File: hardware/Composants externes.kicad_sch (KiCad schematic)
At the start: 0 parts

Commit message: Erreur de manipulation, version 2.3 ok
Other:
- note added: "Nappe communication I2C avec FRDM-IMX8MP ------------------------------------------------------------ Reference Fabriquant qté Remarque IDSD-05-D-03.00-T-G Samtec 1 Nappe IDC 5*2 pins, 3 pouces de long IDSD-05-D-04.00-T-G Samtec 1 Nappe IDC 5*2 pins, 4 pouces de long"
- note removed: "Nappe communication I2C avec FRDM-IMX8MP ------------------------------------------------------------ Reference Fabriquant qté Remarque IDSD-05-D-02.00-T-G Samtec 1 Nappe IDC 5*2 pins, 5cm de long"
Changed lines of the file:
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@@
 		)
 	)
-	(text "Nappe communication I2C avec FRDM-IMX8MP\n------------------------------------------------------------\nReference              Fabriquant       qté          Remarque\nIDSD-05-D-02.00-T-G    Samtec           1            Nappe IDC 5*2 pins, 5cm de long"
+	(text "Nappe communication I2C avec FRDM-IMX8MP\n------------------------------------------------------------\nReference              Fabriquant       qté          Remarque\nIDSD-05-D-03.00-T-G    Samtec           1            Nappe IDC 5*2 pins, 3 pouces de long\nIDSD-05-D-04.00-T-G    Samtec           1            Nappe IDC 5*2 pins, 4 pouces de long"
 		(exclude_from_sim no)
 		(at 19.304 99.568 0)

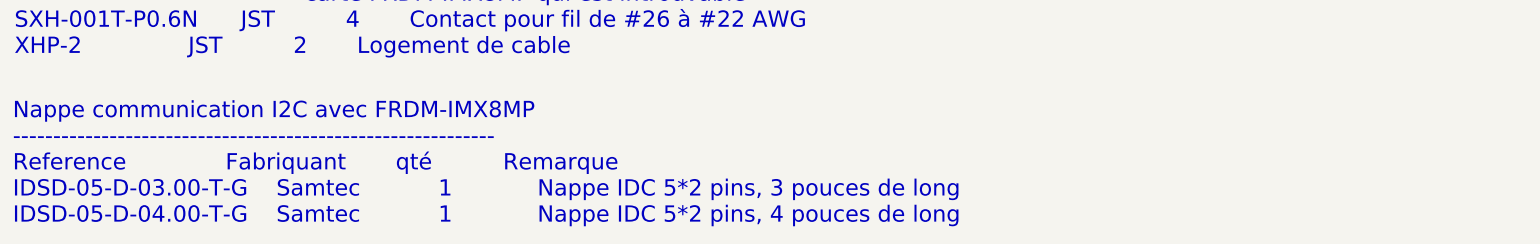
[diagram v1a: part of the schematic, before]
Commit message: V2.3b: correction sur la nomenclature (bom) de plusieurs composants, suppression d'une mauvaise manipulation precedente
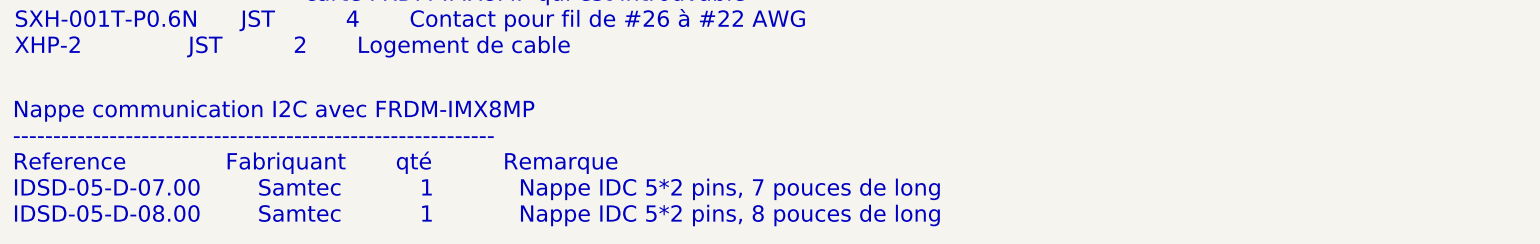
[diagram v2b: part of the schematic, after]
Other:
- note added: "Nappe communication I2C avec FRDM-IMX8MP ------------------------------------------------------------ Reference Fabriquant qté Remarque IDSD-05-D-07.00 Samtec 1 Nappe IDC 5*2 pins, 7 pouces de long IDSD-05-D-08.00 Samtec 1 Nappe IDC 5*2 pins, 8 pouces de long"
- note removed: "Nappe communication I2C avec FRDM-IMX8MP ------------------------------------------------------------ Reference Fabriquant qté Remarque IDSD-05-D-03.00-T-G Samtec 1 Nappe IDC 5*2 pins, 3 pouces de long IDSD-05-D-04.00-T-G Samtec 1 Nappe IDC 5*2 pins, 4 pouces de long"
- company: (none) -> INSA-GEI
- title: (none) -> Composants externes
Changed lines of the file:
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@@
 	(generator_version "8.0")
 	(paper "A4")
+	(title_block
+		(title "Composants externes")
+		(date "2026-09-22")
+		(rev "2.3b")
+		(company "INSA-GEI")
+	)
 	(text "Harnais alimentation Carte FRDM-IMX8MP\n------------------------------------------------------------------------------\nReference           Fabriquant   Qté     Remarque\nB2B-XH-A(LF)(SN)    JST          1       Remplace le connecteur J1 de la\n                                         carte FRDM-IMX8MP qui est introuvable\nSXH-001T-P0.6N      JST          4       Contact pour fil de #26 à #22 AWG\nXHP-2               JST          2       Logement de cable\n\n"
 		(exclude_from_sim no)
@@
 		)
 	)
-	(text "Nappe communication I2C avec FRDM-IMX8MP\n------------------------------------------------------------\nReference              Fabriquant       qté          Remarque\nIDSD-05-D-03.00-T-G    Samtec           1            Nappe IDC 5*2 pins, 3 pouces de long\nIDSD-05-D-04.00-T-G    Samtec           1            Nappe IDC 5*2 pins, 4 pouces de long"
+	(text "Nappe communication I2C avec FRDM-IMX8MP\n------------------------------------------------------------\nReference              Fabriquant       qté          Remarque\nIDSD-05-D-07.00        Samtec           1            Nappe IDC 5*2 pins, 7 pouces de long\nIDSD-05-D-08.00        Samtec           1            Nappe IDC 5*2 pins, 8 pouces de long"
 		(exclude_from_sim no)
 		(at 19.304 99.568 0)
